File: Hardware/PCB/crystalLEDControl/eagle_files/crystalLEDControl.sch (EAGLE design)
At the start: 6 parts

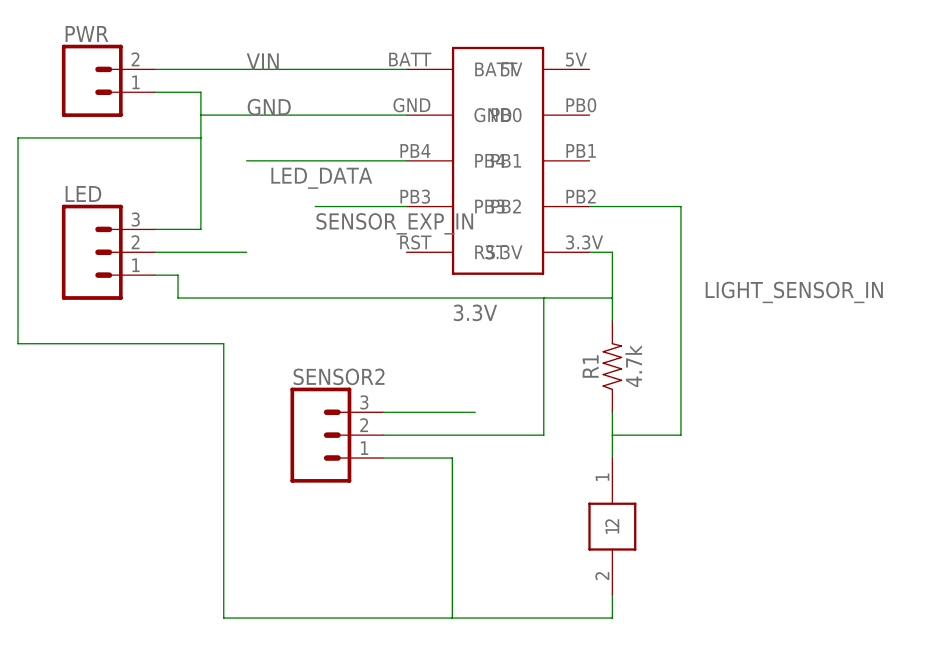
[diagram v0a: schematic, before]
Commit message: Add MIMS microphone and support directly to board.
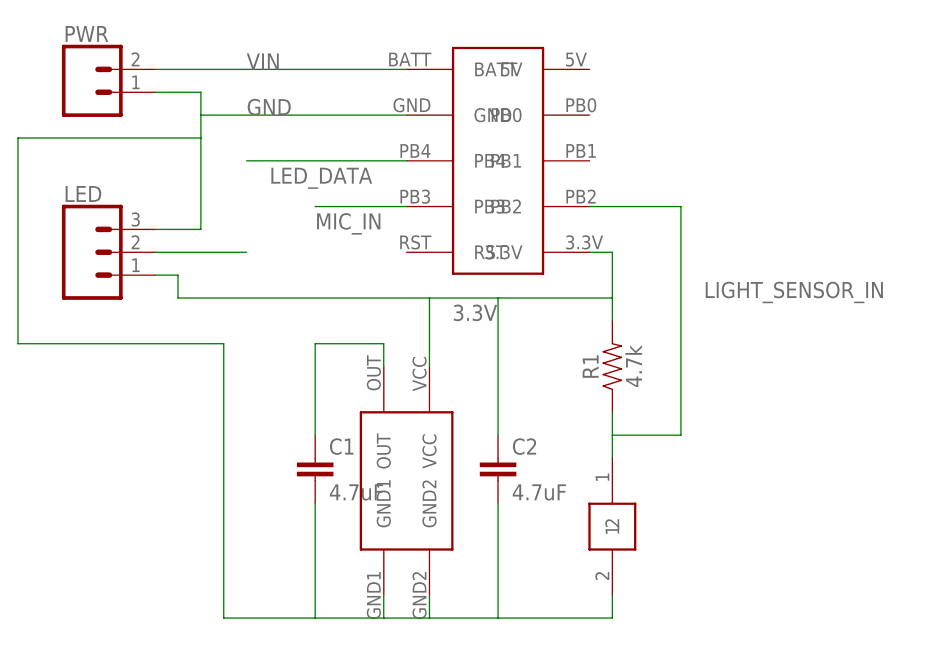
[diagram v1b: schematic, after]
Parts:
- removed SENSOR2: (no value), SparkFun-Connectors:CONN_03
- added A1: (no value), freddyLibr:SPW2430
- added C1, C2: 4.7uF, SparkFun-Capacitors:4.7UF0603
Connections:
- removed net SENSOR_EXP_IN: MCU1.PB3, SENSOR2.3
- new net MIC_IN: A1.OUT, C1.1, MCU1.PB3
- net 3.3V: now also A1.VCC, C2.1; no longer SENSOR2.2
- net GND: now also A1.GND1, A1.GND2, C1.2, C2.2; no longer SENSOR2.1
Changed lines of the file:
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@@
 <part name="R1" library="SparkFun-Resistors" deviceset="4.7KOHM" device="-0603-1/10W-1%" value="4.7k"/>
 <part name="PC1" library="freddyLibr" deviceset="PDV-P8101" device=""/>
-<part name="SENSOR2" library="SparkFun-Connectors" deviceset="CONN_03" device=""/>
+<part name="A1" library="freddyLibr" deviceset="SPW2430" device=""/>
+<part name="C1" library="SparkFun-Capacitors" deviceset="4.7UF" device="0603" value="4.7uF"/>
+<part name="C2" library="SparkFun-Capacitors" deviceset="4.7UF" device="0603" value="4.7uF"/>
 </parts>
 <sheets>
@@
 <instance part="R1" gate="G$1" x="78.74" y="25.4" rot="R90"/>
 <instance part="PC1" gate="G$1" x="78.74" y="7.62"/>
-<instance part="SENSOR2" gate="J$1" x="45.72" y="17.78"/>
+<instance part="A1" gate="G$1" x="55.88" y="12.7"/>
+<instance part="C1" gate="G$1" x="45.72" y="12.7"/>
+<instance part="C2" gate="G$1" x="66.04" y="12.7"/>
 </instances>
 <busses>
@@
 <wire x1="76.2" y1="38.1" x2="78.74" y2="38.1" width="0.1524" layer="91"/>
 <wire x1="78.74" y1="38.1" x2="78.74" y2="33.02" width="0.1524" layer="91"/>
-<wire x1="78.74" y1="33.02" x2="71.12" y2="33.02" width="0.1524" layer="91"/>
 <pinref part="R1" gate="G$1" pin="2"/>
 <wire x1="78.74" y1="33.02" x2="78.74" y2="30.48" width="0.1524" layer="91"/>
-<pinref part="SENSOR2" gate="J$1" pin="2"/>
-<wire x1="53.34" y1="17.78" x2="71.12" y2="17.78" width="0.1524" layer="91"/>
-<wire x1="71.12" y1="17.78" x2="71.12" y2="33.02" width="0.1524" layer="91"/>
 <label x="60.96" y="30.48" size="1.778" layer="95"/>
-<wire x1="71.12" y1="33.02" x2="30.48" y2="33.02" width="0.1524" layer="91"/>
+<wire x1="78.74" y1="33.02" x2="66.04" y2="33.02" width="0.1524" layer="91"/>
+<wire x1="66.04" y1="33.02" x2="58.42" y2="33.02" width="0.1524" layer="91"/>
+<wire x1="58.42" y1="33.02" x2="30.48" y2="33.02" width="0.1524" layer="91"/>
 <wire x1="30.48" y1="33.02" x2="30.48" y2="35.56" width="0.1524" layer="91"/>
 <pinref part="LED" gate="J$1" pin="1"/>
 <wire x1="30.48" y1="35.56" x2="27.94" y2="35.56" width="0.1524" layer="91"/>
+<wire x1="58.42" y1="33.02" x2="58.42" y2="25.4" width="0.1524" layer="91"/>
+<pinref part="A1" gate="G$1" pin="VCC"/>
+<pinref part="C2" gate="G$1" pin="1"/>
+<wire x1="66.04" y1="33.02" x2="66.04" y2="17.78" width="0.1524" layer="91"/>
 </segment>
 </net>
@@
 <pinref part="PC1" gate="G$1" pin="2"/>
 <wire x1="78.74" y1="0" x2="78.74" y2="-2.54" width="0.1524" layer="91"/>
-<wire x1="78.74" y1="-2.54" x2="60.96" y2="-2.54" width="0.1524" layer="91"/>
-<wire x1="60.96" y1="-2.54" x2="35.56" y2="-2.54" width="0.1524" layer="91"/>
+<wire x1="78.74" y1="-2.54" x2="66.04" y2="-2.54" width="0.1524" layer="91"/>
+<wire x1="66.04" y1="-2.54" x2="58.42" y2="-2.54" width="0.1524" layer="91"/>
+<wire x1="58.42" y1="-2.54" x2="53.34" y2="-2.54" width="0.1524" layer="91"/>
+<wire x1="53.34" y1="-2.54" x2="45.72" y2="-2.54" width="0.1524" layer="91"/>
+<wire x1="45.72" y1="-2.54" x2="35.56" y2="-2.54" width="0.1524" layer="91"/>
 <wire x1="35.56" y1="-2.54" x2="35.56" y2="27.94" width="0.1524" layer="91"/>
 <wire x1="35.56" y1="27.94" x2="12.7" y2="27.94" width="0.1524" layer="91"/>
@@
 <wire x1="33.02" y1="50.8" x2="33.02" y2="53.34" width="0.1524" layer="91"/>
 <label x="38.1" y="53.34" size="1.778" layer="95"/>
-<pinref part="SENSOR2" gate="J$1" pin="1"/>
-<wire x1="53.34" y1="15.24" x2="60.96" y2="15.24" width="0.1524" layer="91"/>
-<wire x1="60.96" y1="15.24" x2="60.96" y2="-2.54" width="0.1524" layer="91"/>
 <wire x1="33.02" y1="50.8" x2="33.02" y2="40.64" width="0.1524" layer="91"/>
 <pinref part="LED" gate="J$1" pin="3"/>
 <wire x1="33.02" y1="40.64" x2="27.94" y2="40.64" width="0.1524" layer="91"/>
+<wire x1="53.34" y1="0" x2="53.34" y2="-2.54" width="0.1524" layer="91"/>
+<wire x1="58.42" y1="0" x2="58.42" y2="-2.54" width="0.1524" layer="91"/>
+<pinref part="A1" gate="G$1" pin="GND1"/>
+<pinref part="A1" gate="G$1" pin="GND2"/>
+<pinref part="C1" gate="G$1" pin="2"/>
+<wire x1="45.72" y1="10.16" x2="45.72" y2="-2.54" width="0.1524" layer="91"/>
+<pinref part="C2" gate="G$1" pin="2"/>
+<wire x1="66.04" y1="10.16" x2="66.04" y2="-2.54" width="0.1524" layer="91"/>
 </segment>
 </net>
@@
 </segment>
 </net>
-<net name="SENSOR_EXP_IN" class="0">
+<net name="MIC_IN" class="0">
+<segment>
+<pinref part="A1" gate="G$1" pin="OUT"/>
+<wire x1="53.34" y1="25.4" x2="53.34" y2="27.94" width="0.1524" layer="91"/>
+<wire x1="53.34" y1="27.94" x2="45.72" y2="27.94" width="0.1524" layer="91"/>
+<pinref part="C1" gate="G$1" pin="1"/>
+<wire x1="45.72" y1="27.94" x2="45.72" y2="17.78" width="0.1524" layer="91"/>
+</segment>
 <segment>
 <pinref part="MCU1" gate="G$1" pin="PB3"/>
@@
 <label x="45.72" y="40.64" size="1.778" layer="95"/>
 </segment>
-<segment>
-<pinref part="SENSOR2" gate="J$1" pin="3"/>
-<wire x1="53.34" y1="20.32" x2="63.5" y2="20.32" width="0.1524" layer="91"/>
-</segment>
 </net>
